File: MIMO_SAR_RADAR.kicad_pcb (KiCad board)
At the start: 2 copper layers, 37 parts, among them IC1 SKY13418-485LF, IC10 PSA2-6+, IC11 ADL5380ACPZ-R7, IC12 ADL5380ACPZ-R7, IC13 ADL5380ACPZ-R7, IC14 ADL5380ACPZ-R7, IC15 SKY13418-485LF, IC16 ADA4940-2ACPZ-RL, IC17 ADA4940-2ACPZ-RL, IC18 ADA4940-2ACPZ-RL, IC19 ADA4940-2ACPZ-RL, IC2 SKY13418-485LF, IC20 ADS8588SIPM, IC3 SKY13418-485LF, IC4 SKY13418-485LF, IC5 LMX2572RHAT, IC6 PMA3-73-1W+, IC7 PSA2-6+, IC8 PSA2-6+, IC9 PSA2-6+, U1 MAX5035AUSA, U2 STM32H7A3IGTx, U3 ESP32-C3-WROOM-02, U4 TSR2-24120, Y1 SiT9121AI-2B1-33E100.000000G

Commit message: work...
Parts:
- added IC21: LMX2594RHAT, LMX:QFN50P600X600X100-41N-D, F.Cu at (26.2, 88.0)
- added IC22: SKY13418-485LF, SKY13:SKY13418485LF, F.Cu at (24.7, 81.1)
- added IC23: SKY13418-485LF, SKY13:SKY13418485LF, F.Cu at (30.1, 81.1)
- added IC5: LT3042IMSE#PBF, Low_noise_LDO:SOP50P490X110-11N, F.Cu at (34.0, 86.1)
- added L1: XFL4020-222MEB, XFL4020-222:XFL4020-222ME, F.Cu at (33.6, 91.0)
- added PS1: TPS62150RGTR, TPS62150:QFN50P300X300X100-17N-D, F.Cu at (35.4, 81.0)
- moved U2 9.08 mm to (50.0, 47.4)
- moved IC5 1.26 mm to (66.0, 83.5)
- moved IC12 1.21 mm to (87.7, 75.4)
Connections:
- FL1 pad 4: GND -> unconnected-(FL1-GROUND_2-Pad4)
- FL10 pad 1: unconnected-(FL10-INPUT-Pad1) -> Net-(FL10-INPUT)
- FL10 pad 2: unconnected-(FL10-GROUND_1-Pad2) -> GND
- FL10 pad 3: unconnected-(FL10-OUTPUT-Pad3) -> Net-(FL10-OUTPUT)
- FL10 pad 4: unconnected-(FL10-GROUND_2-Pad4) -> GND
- FL10 pad 5: unconnected-(FL10-GROUND_3-Pad5) -> GND
- FL10 pad 6: unconnected-(FL10-GROUND_4-Pad6) -> GND
- FL8 pad 4: GND -> Net-(FL8-GROUND_2)
- FL8 pad 5: GND -> Net-(FL8-GROUND_2)
- FL8 pad 6: GND -> Net-(FL8-GROUND_2)
- FL9 pad 1: unconnected-(FL9-RF_IN-Pad1) -> Net-(FL9-RF_IN)
- FL9 pad 2: unconnected-(FL9-GROUND_1-Pad2) -> GND
- FL9 pad 3: unconnected-(FL9-RF_OUT-Pad3) -> Net-(FL10-INPUT)
- FL9 pad 4: unconnected-(FL9-GROUND_2-Pad4) -> GND
- HMC476MP86(FREQUENZBEREICH)1 pad 1: unconnected-(HMC476MP86(FREQUENZBEREICH)1-RF_IN-Pad1) -> Net-(HMC476MP86(FREQUENZBEREICH)1-RF_IN)
- HMC476MP86(FREQUENZBEREICH)1 pad 2: unconnected-(HMC476MP86(FREQUENZBEREICH)1-GND_1-Pad2) -> GND
- HMC476MP86(FREQUENZBEREICH)1 pad 3: unconnected-(HMC476MP86(FREQUENZBEREICH)1-RF-OUT_AND_DC-IN-Pad3) -> Net-(HMC476MP86(FREQUENZBEREICH)1-RF-OUT_AND_DC-IN)
- HMC476MP86(FREQUENZBEREICH)1 pad 4: unconnected-(HMC476MP86(FREQUENZBEREICH)1-GND_2-Pad4) -> GND
- IC15 pad 13: unconnected-(IC15-ANT-Pad13) -> Net-(IC15-ANT)
- IC15 pad 15: unconnected-(IC15-GND-Pad15) -> GND
- IC15 pad 5: unconnected-(IC15-V3-Pad5) -> RF_SWITCH_BIT_3
- IC15 pad 6: unconnected-(IC15-V2-Pad6) -> RF_SWITCH_BIT_2
- IC15 pad 7: unconnected-(IC15-V1-Pad7) -> RF_SWITCH_BIT_1
- IC6 pad 1: unconnected-(IC6-GND_1-Pad1) -> GND
- IC6 pad 12: unconnected-(IC6-VIADJ-Pad12) -> Net-(IC6-VIADJ)
- IC6 pad 13: unconnected-(IC6-EP-Pad13) -> GND
- IC6 pad 2: unconnected-(IC6-RF-IN-Pad2) -> Net-(HMC476MP86(FREQUENZBEREICH)1-RF-OUT_AND_DC-IN)
- IC6 pad 3: unconnected-(IC6-GND_2-Pad3) -> GND
- IC6 pad 7: unconnected-(IC6-GND_3-Pad7) -> GND
- IC6 pad 8: unconnected-(IC6-RF-OUT+VDD-Pad8) -> Net-(FL9-RF_IN)
- IC6 pad 9: unconnected-(IC6-GND_4-Pad9) -> GND
- TDK_HHM2952A1/auf_PCB1 pad 1: unconnected-(TDK_HHM2952A1/auf_PCB1-Input-Pad1) -> Net-(FL10-OUTPUT)
- TDK_HHM2952A1/auf_PCB1 pad 3: Net-(TDK_HHM2952A1/auf_PCB1-GND-Pad3) -> GND
- TDK_HHM2952A1/auf_PCB1 pad 4: Net-(TDK_HHM2952A1/auf_PCB1-GND-Pad3) -> GND
- U2 pad 120: unconnected-(U2-PA9-Pad120) -> RF_SWITCH_BIT_1
- U2 pad 121: unconnected-(U2-PA10-Pad121) -> RF_SWITCH_BIT_2
- U2 pad 122: unconnected-(U2-PA11-Pad122) -> RF_SWITCH_BIT_3
- U2 pad 50: unconnected-(U2-PA4-Pad50) -> SS
- U2 pad 51: unconnected-(U2-PA5-Pad51) -> CLOCK
- U2 pad 53: unconnected-(U2-PA7-Pad53) -> MOSI
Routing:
- net unconnected-(IC15-RF8-Pad12): track 0.00 -> 9.35 mm

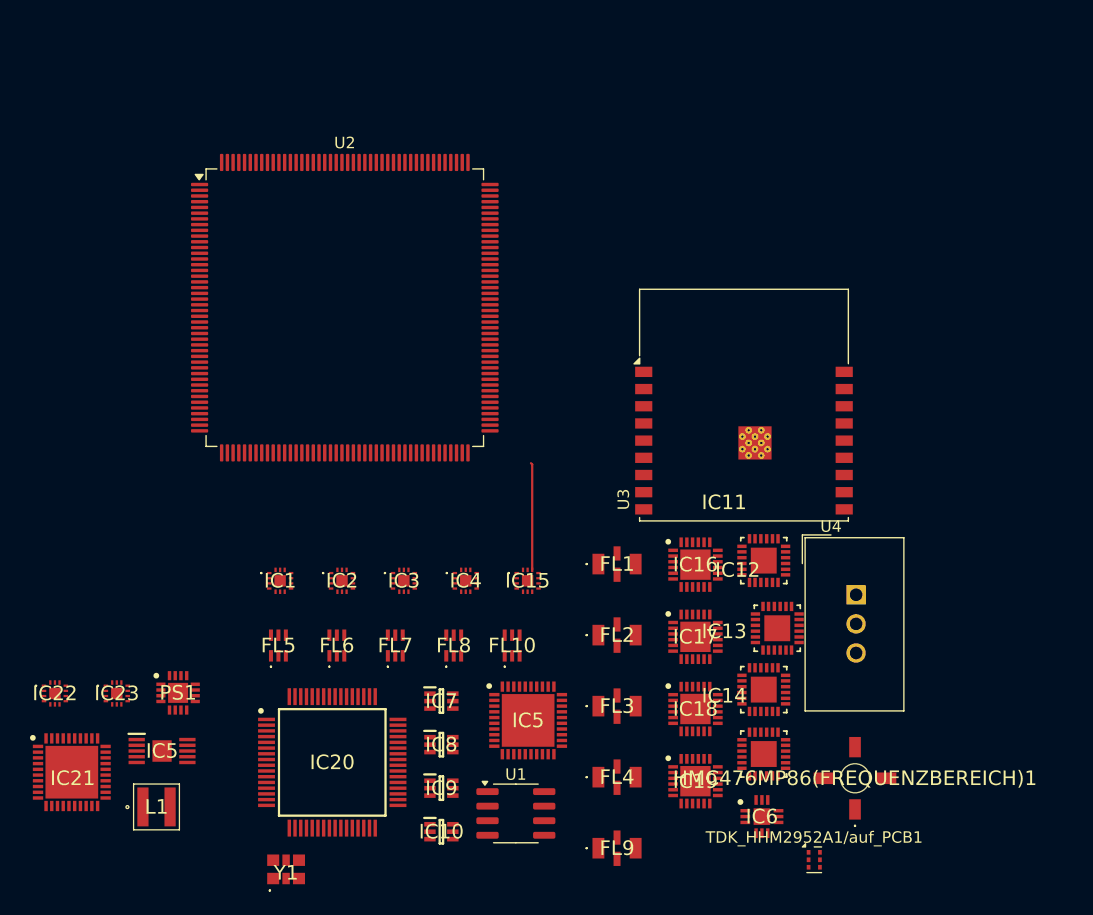
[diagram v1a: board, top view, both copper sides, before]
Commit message: Structure +2.nd rx channel
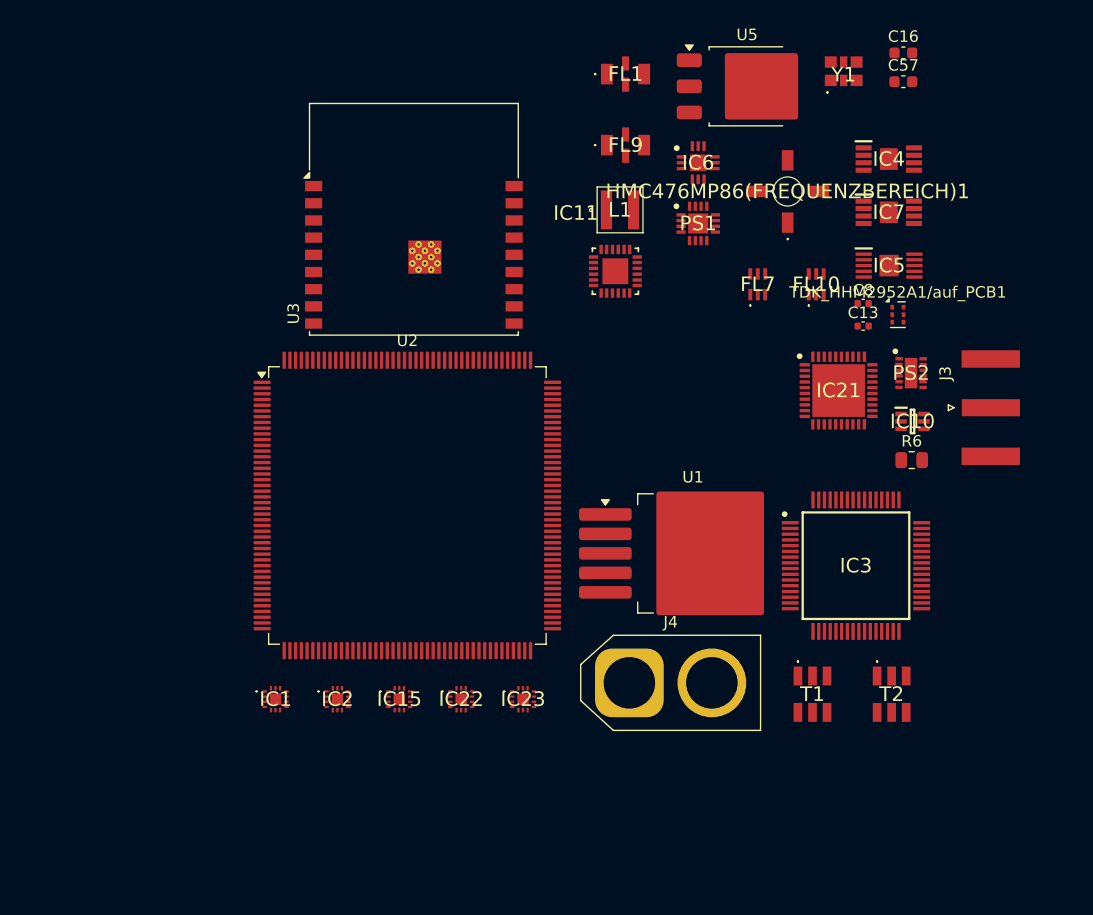
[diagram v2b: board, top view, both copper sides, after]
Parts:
- removed FL2, FL3, FL4: LFCN-6000+, RF_LP:LFCN6000
- removed FL5, FL6, FL8: HFCG-3000+, RF_HP:HFCG3000
- removed IC12, IC13, IC14: ADL5380ACPZ-R7, RF_Modulators:QFN50P400X400X100-25N
- removed IC16, IC17, IC18, IC19: ADA4940-2ACPZ-RL, ADC_DRIVER:QFN50P400X400X80-25N-D
- removed IC20: ADS8588SIPM, HS_ADC:QFP50P1200X1200X160-64N
- removed the IC5 at (34.0, 86.1)
- removed the IC5 at (66.0, 83.5)
- removed IC8, IC9: PSA2-6+, LNA:SOT65P215X100-6N
- removed U4: TSR2-24120, Converter_DCDC:Converter_DCDC_TRACO_TSR2-xxxx_THT
- added C13: 100pF, Capacitor_SMD:C_0402_1005Metric, F.Cu at (95.2, 49.0)
- added C16: 0.1uF, Capacitor_SMD:C_0603_1608Metric, F.Cu at (98.8, 25.2)
- added C57: 0.01uF, Capacitor_SMD:C_0603_1608Metric, F.Cu at (98.8, 27.7)
- added C8: 100pF, Capacitor_SMD:C_0402_1005Metric, F.Cu at (95.2, 47.1)
- added IC5: LT3042IMSE#PBF, Low_noise_LDO:SOP50P490X110-11N, F.Cu at (97.5, 43.8)
- added J3: Conn_Coaxial_Small, Connector_Coaxial:SMA_Amphenol_132289_EdgeMount, F.Cu at (106.4, 56.2)
- added J4: Conn_01x02_Pin, Connector_AMASS:AMASS_XT60-F_1x02_P7.20mm_Vertical, F.Cu at (74.8, 80.2)
- added PS2: LM27762DSSR, LM27762DSSR:SON50P200X300X80-13N-D, F.Cu at (99.4, 53.1)
- added R6: 93.1R, Resistor_SMD:R_0805_2012Metric, F.Cu at (99.5, 60.7)
- added T1: TCM1-63AX-2+, Balun:TCM163AX2, F.Cu at (90.8, 81.2)
- added T2: TCM1-63AX-2+, Balun:TCM163AX2, F.Cu at (97.7, 81.2)
- added U5: LM1117DT-3.3, Package_TO_SOT_SMD:TO-252-3_TabPin2, F.Cu at (85.1, 28.1)
- IC3: value SKY13418-485LF -> ADS8584SIPM; footprint SKY13:SKY13418485LF -> 4CH_ADC:QFP50P1200X1200X160-64N
- IC4: value SKY13418-485LF -> OPA1632DGNR; footprint SKY13:SKY13418485LF -> DIFF_AMPS:SOP65P490X110-9N
- IC7: value PSA2-6+ -> OPA1632DGNR; footprint LNA:SOT65P215X100-6N -> DIFF_AMPS:SOP65P490X110-9N
- U1: value MAX5035AUSA -> LM2596S-12; footprint Package_SO:SOIC-8_3.9x4.9mm_P1.27mm -> Package_TO_SOT_SMD:TO-263-5_TabPin3
- moved Y1 85.0 mm to (93.5, 26.8)
- moved IC21 74.8 mm to (93.1, 54.7)
- moved L1 66.0 mm to (74.0, 38.9)
- moved FL9 61.4 mm to (74.5, 33.2)
- moved PS1 61.1 mm to (80.8, 40.1)
- moved IC7 57.8 mm to (97.5, 39.1)
- moved IC6 57.3 mm to (80.8, 34.8)
- moved IC10 54.5 mm to (99.5, 57.4)
- moved IC4 52.1 mm to (97.5, 34.5)
- moved HMC476MP86(FREQUENZBEREICH)1 51.6 mm to (88.7, 37.3)
- moved TDK_HHM2952A1/auf_PCB1 48.1 mm to (98.3, 48.0)
- moved FL7 44.7 mm to (86.0, 45.4)
- moved FL1 42.8 mm to (74.5, 27.0)
- moved FL10 41.2 mm to (91.1, 45.4)
- moved IC3 39.5 mm to (94.6, 69.9)
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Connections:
- FL1 pad 1: unconnected-(FL1-RF_IN-Pad1) -> Net-(FL1-RF_IN)
- FL1 pad 3: unconnected-(FL1-RF_OUT-Pad3) -> Net-(FL1-RF_OUT)
- FL1 pad 4: unconnected-(FL1-GROUND_2-Pad4) -> GND
- FL7 pad 1: unconnected-(FL7-INPUT-Pad1) -> Net-(FL1-RF_OUT)
- FL7 pad 3: unconnected-(FL7-OUTPUT-Pad3) -> Net-(FL7-OUTPUT)
- IC1 pad 13: unconnected-(IC1-ANT-Pad13) -> Net-(FL1-RF_IN)
- IC1 pad 15: unconnected-(IC1-GND-Pad15) -> GND
- IC1 pad 4: unconnected-(IC1-VDD-Pad4) -> +3.3V
- IC1 pad 5: unconnected-(IC1-V3-Pad5) -> RX1_B2
- IC1 pad 6: unconnected-(IC1-V2-Pad6) -> RX1_B1
- IC1 pad 7: unconnected-(IC1-V1-Pad7) -> RX1_B0
- IC10 pad 1: unconnected-(IC10-RF-IN-Pad1) -> Net-(IC10-RF-IN)
- IC10 pad 2: unconnected-(IC10-GND_1-Pad2) -> GND
- IC10 pad 3: unconnected-(IC10-GND_2-Pad3) -> GND
- IC10 pad 4: unconnected-(IC10-RF-OUT_&_VD-Pad4) -> Net-(IC10-RF-OUT_&_VD)
- IC10 pad 5: unconnected-(IC10-GND_3-Pad5) -> GND
- IC10 pad 6: unconnected-(IC10-GND_4-Pad6) -> GND
- IC11 pad 1: unconnected-(IC11-GND3_2-Pad1) -> GND
- IC11 pad 10: unconnected-(IC11-LOIN-Pad10) -> Net-(IC11-LOIN)
- IC11 pad 11: unconnected-(IC11-GND4-Pad11) -> GND
- IC11 pad 13: unconnected-(IC11-VCC2-Pad13) -> 5V_CLEAN
- IC11 pad 14: unconnected-(IC11-GND2_2-Pad14) -> GND
- IC11 pad 15: unconnected-(IC11-QLO-Pad15) -> Net-(IC11-QLO)
- IC11 pad 16: unconnected-(IC11-QHI-Pad16) -> Net-(IC11-QHI)
- IC11 pad 17: unconnected-(IC11-GND2-Pad17) -> GND
- IC11 pad 18: unconnected-(IC11-GND3_3-Pad18) -> GND
- IC11 pad 19: unconnected-(IC11-ADJ-Pad19) -> Net-(IC11-ADJ)
- IC11 pad 2: unconnected-(IC11-GND1_2-Pad2) -> GND
- IC11 pad 20: unconnected-(IC11-GND3_4-Pad20) -> GND
- IC11 pad 21: unconnected-(IC11-REFIN-Pad21) -> Net-(IC11-REFIN)
- IC11 pad 22: unconnected-(IC11-REFIP-Pad22) -> Net-(IC11-REFIP)
- IC11 pad 23: unconnected-(IC11-GND3-Pad23) -> GND
- IC11 pad 24: unconnected-(IC11-VDD3-Pad24) -> 5V_CLEAN
- IC11 pad 3: unconnected-(IC11-IHI-Pad3) -> IHI1
- IC11 pad 4: unconnected-(IC11-ILO-Pad4) -> ILO1
- IC11 pad 5: unconnected-(IC11-GND1-Pad5) -> GND
- IC11 pad 6: unconnected-(IC11-VCC1-Pad6) -> 5V_CLEAN
- IC11 pad 7: unconnected-(IC11-ENBL-Pad7) -> Net-(IC11-ENBL)
- IC11 pad 8: unconnected-(IC11-GND4_2-Pad8) -> GND
- IC11 pad 9: unconnected-(IC11-LOIP-Pad9) -> Net-(IC11-LOIP)
- IC15 pad 4: unconnected-(IC15-VDD-Pad4) -> +3.3V
- IC2 pad 15: unconnected-(IC2-GND-Pad15) -> GND
- IC2 pad 4: unconnected-(IC2-VDD-Pad4) -> +3.3V
- IC2 pad 5: unconnected-(IC2-V3-Pad5) -> RX2_B2
- IC2 pad 6: unconnected-(IC2-V2-Pad6) -> RX2_B1
- IC2 pad 7: unconnected-(IC2-V1-Pad7) -> RX2_B0
- IC21 pad 23: Net-(HMC476MP86(FREQUENZBEREICH)1-RF_IN) -> Net-(IC21-RFOUTAP)
- IC22 pad 4: unconnected-(IC22-VDD-Pad4) -> +3.3V
- IC23 pad 13: unconnected-(IC23-ANT-Pad13) -> Net-(IC23-ANT)
- IC23 pad 4: unconnected-(IC23-VDD-Pad4) -> +3.3V
- IC23 pad 6: unconnected-(IC23-V2-Pad6) -> Net-(IC23-V2)
- IC23 pad 7: unconnected-(IC23-V1-Pad7) -> Net-(IC23-V1)
- IC4 pad 1: unconnected-(IC4-RF5-Pad1) -> Net-(IC4-VIN-)
- IC4 pad 2: unconnected-(IC4-RF3-Pad2) -> GND
- IC4 pad 7: unconnected-(IC4-V1-Pad7) -> Net-(IC4-ENABLE)
- IC4 pad 8: unconnected-(IC4-N/C-Pad8) -> Net-(IC4-VIN+)
- IC4 pad 9: unconnected-(IC4-RF2-Pad9) -> GND
- IC6 pad 2: Net-(HMC476MP86(FREQUENZBEREICH)1-RF-OUT_AND_DC-IN) -> Net-(IC6-RF-IN)
- IC7 pad 1: unconnected-(IC7-RF-IN-Pad1) -> Net-(IC7-VIN-)
- IC7 pad 2: unconnected-(IC7-GND_1-Pad2) -> GND
- TDK_HHM2952A1/auf_PCB1 pad 2: unconnected-(TDK_HHM2952A1/auf_PCB1-Coupled-Pad2) -> SPLIT_TX
- TDK_HHM2952A1/auf_PCB1 pad 5: unconnected-(TDK_HHM2952A1/auf_PCB1-Isolated-Pad5) -> Net-(TDK_HHM2952A1/auf_PCB1-Isolated)
- TDK_HHM2952A1/auf_PCB1 pad 6: unconnected-(TDK_HHM2952A1/auf_PCB1-Direct-Pad6) -> Net-(J3-In)
- U1 pad 1: unconnected-(U1-BST-Pad1) -> Net-(D3-K)
- U1 pad 2: unconnected-(U1-VD-Pad2) -> Net-(D2-K)
- U1 pad 3: unconnected-(U1-SGND-Pad3) -> GND
- U1 pad 4: unconnected-(U1-FB-Pad4) -> Net-(U1-FB)
- U1 pad 5: unconnected-(U1-ON/~{OFF}-Pad5) -> GND
- U2 pad 102: Net-(U2-VSS-Pad102) -> GND
- U2 pad 103: unconnected-(U2-VDD-Pad103) -> +3.3V
- U2 pad 113: Net-(U2-VSS-Pad102) -> GND
- U2 pad 126: Net-(U2-VSS-Pad102) -> GND
- U2 pad 127: unconnected-(U2-VDD-Pad127) -> +3.3V
- U2 pad 135: Net-(U2-VSS-Pad102) -> GND
- U2 pad 136: unconnected-(U2-VDD-Pad136) -> +3.3V
- U2 pad 14: Net-(U2-VSS-Pad102) -> GND
- U2 pad 148: Net-(U2-VSS-Pad102) -> GND
- U2 pad 15: unconnected-(U2-VDD-Pad15) -> +3.3V
- U2 pad 158: Net-(U2-VSS-Pad102) -> GND
- U2 pad 159: unconnected-(U2-VDD-Pad159) -> +3.3V
- U2 pad 172: unconnected-(U2-VDD-Pad172) -> +3.3V
- U2 pad 22: Net-(U2-VSS-Pad102) -> GND
- U2 pad 23: unconnected-(U2-VDD-Pad23) -> +3.3V
- U2 pad 36: unconnected-(U2-VDD-Pad36) -> +3.3V
- U2 pad 37: unconnected-(U2-VSSA-Pad37) -> GND
- U2 pad 48: Net-(U2-VSS-Pad102) -> GND
- U2 pad 49: unconnected-(U2-VDD-Pad49) -> +3.3V
- U2 pad 61: Net-(U2-VSS-Pad102) -> GND
- U2 pad 62: unconnected-(U2-VDD-Pad62) -> +3.3V
- U2 pad 71: Net-(U2-VSS-Pad102) -> GND
- U2 pad 72: unconnected-(U2-VDD-Pad72) -> +3.3V
- U2 pad 82: unconnected-(U2-VDD-Pad82) -> +3.3V
- U2 pad 90: Net-(U2-VSS-Pad102) -> GND
- U2 pad 91: unconnected-(U2-VDD-Pad91) -> +3.3V
- U3 pad 19: Net-(U3-GND-Pad19) -> GND
- U3 pad 9: Net-(U3-GND-Pad19) -> GND
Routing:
- net unconnected-(IC15-RF8-Pad12): track 9.35 -> 0.00 mm

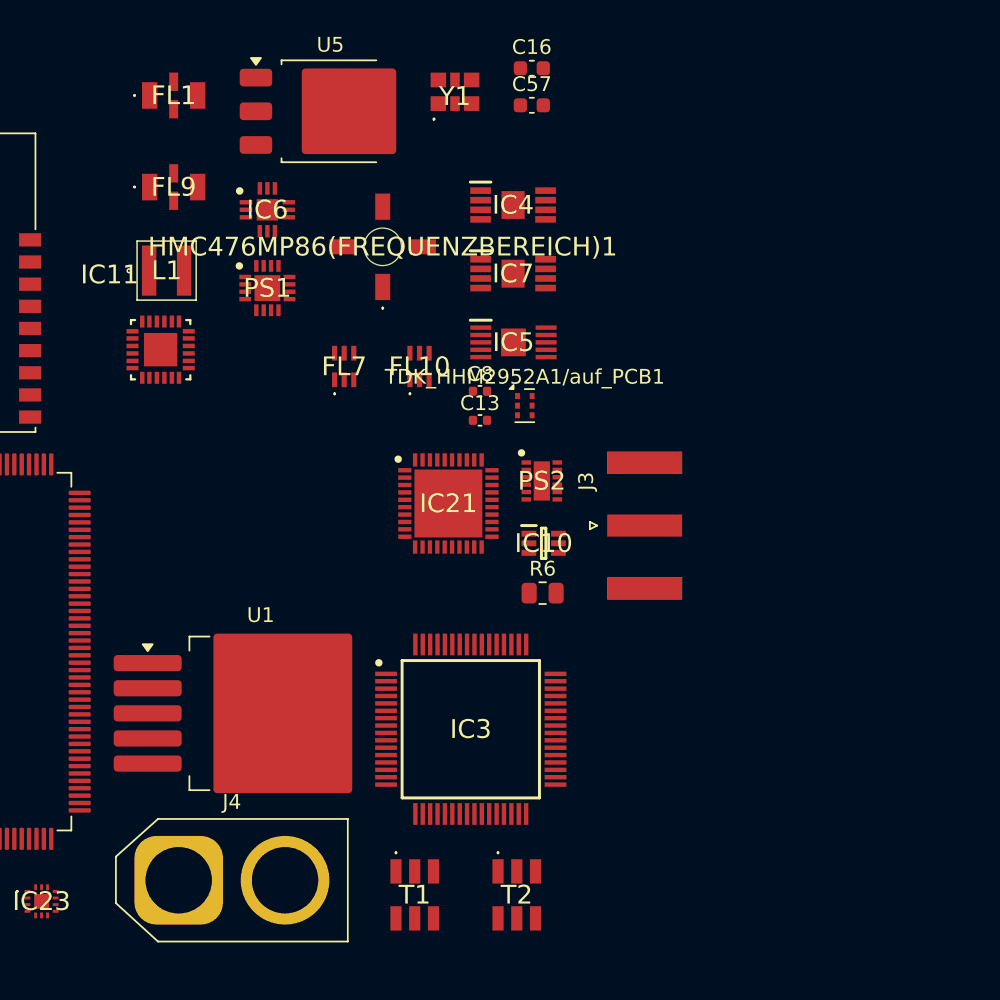
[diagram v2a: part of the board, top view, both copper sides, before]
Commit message: better adc, easyer rx chain design
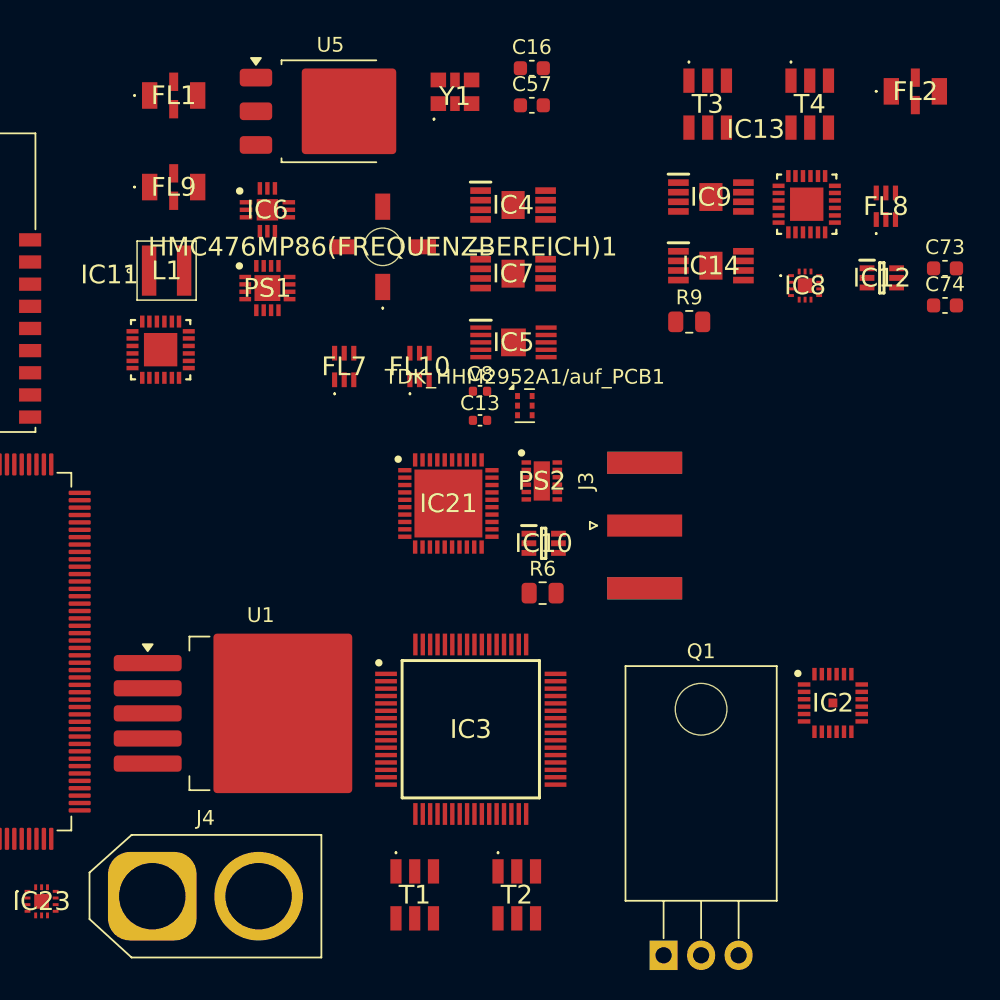
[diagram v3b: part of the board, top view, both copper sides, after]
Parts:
- added C73: 0.01uF, Capacitor_SMD:C_0603_1608Metric, F.Cu at (126.7, 38.7)
- added C74: 0.1uF, Capacitor_SMD:C_0603_1608Metric, F.Cu at (126.7, 41.2)
- added FL2: LFCN-6000+, RF_LP:LFCN6000, F.Cu at (124.7, 26.8)
- added FL8: HFCG-3000+, RF_HP:HFCG3000, F.Cu at (122.7, 34.5)
- added IC12: PSA2-6+, LNA:SOT65P215X100-6N, F.Cu at (122.4, 39.4)
- added IC13: ADL5380ACPZ-R7, RF_Modulators:QFN50P400X400X100-25N, F.Cu at (117.4, 34.4)
- added IC14: OPA1632DGNR, DIFF_AMPS:SOP65P490X110-9N, F.Cu at (110.9, 38.6)
- added IC2: AD7380-4BCPZ, AD7380:QFN50P400X400X60-25N-D, F.Cu at (119.1, 68.2)
- added IC8: SKY13418-485LF, SKY13:SKY13418485LF, F.Cu at (117.2, 39.9)
- added IC9: OPA1632DGNR, DIFF_AMPS:SOP65P490X110-9N, F.Cu at (110.9, 33.9)
- added Q1: D44VH10, Package_TO_SOT_THT:TO-220-3_Horizontal_TabDown, F.Cu at (107.7, 85.2)
- added R9: 93.1R, Resistor_SMD:R_0805_2012Metric, F.Cu at (109.4, 42.4)
- added T3: TCM1-63AX-2+, Balun:TCM163AX2, F.Cu at (110.7, 27.6)
- added T4: TCM1-63AX-2+, Balun:TCM163AX2, F.Cu at (117.6, 27.6)
- J4: footprint Connector_AMASS:AMASS_XT60-F_1x02_P7.20mm_Vertical -> Connector_AMASS:AMASS_XT60-M_1x02_P7.20mm_Vertical
- moved J4 2.09 mm to (73.0, 81.2)
